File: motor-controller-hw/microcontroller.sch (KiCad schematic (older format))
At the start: 0 parts

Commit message: added more signals and parts
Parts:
- added U?: STM32F303RETx, Package_QFP:LQFP-64_10x10mm_P0.5mm, symbol MotorControllerParts:STM32F303RETx
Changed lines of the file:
@@
 Comment4 ""
 $EndDescr
+$Comp
+L MotorControllerParts:STM32F303RETx U?
+U 1 1 5BC0BBCA
+P 5950 3050
+F 0 "U?" H 5950 3050 50  0000 C CNN
+F 1 "STM32F303RETx" H 5950 2950 50  0000 C CNN
+F 2 "Package_QFP:LQFP-64_10x10mm_P0.5mm" H 5350 1350 50  0001 R CNN
+F 3 "http://www.st.com/st-web-ui/static/active/en/resource/technical/document/datasheet/DM00118585.pdf" H 5950 3050 50  0001 C CNN
+	1    5950 3050
+	1    0    0    -1
+$EndComp
 $EndSCHEMATC

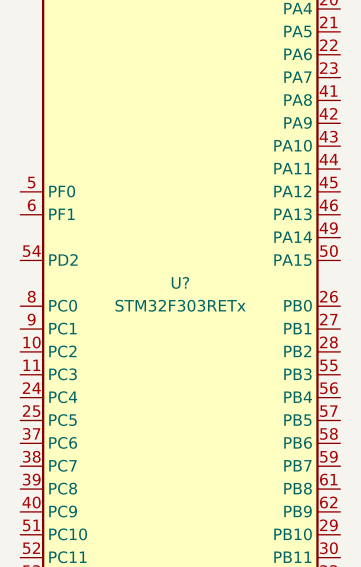
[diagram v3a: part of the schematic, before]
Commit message: Finished Input Protection Added annotations to the title block
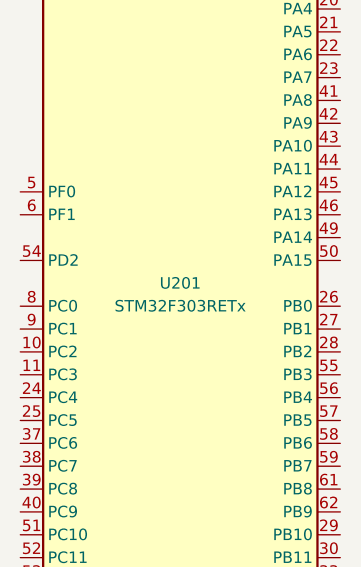
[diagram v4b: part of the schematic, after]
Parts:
- gave numbers to parts that had none: 1
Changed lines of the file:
@@
 $Descr A4 11693 8268
 encoding utf-8
-Sheet 3 5
+Sheet 2 5
 Title ""
 Date ""
 Rev ""
 Comp "Cedarville University"
-Comment1 ""
-Comment2 ""
-Comment3 ""
+Comment1 "Supermileage Motor Controller"
+Comment2 "Senior Design 2018-2019"
+Comment3 "Samuel Ellicott"
 Comment4 ""
 $EndDescr
 $Comp
-L MotorControllerParts:STM32F303RETx U?
+L MotorControllerParts:STM32F303RETx U201
 U 1 1 5BC0BBCA
 P 5950 3050
-F 0 "U?" H 5950 3050 50  0000 C CNN
+F 0 "U201" H 5950 3050 50  0000 C CNN
 F 1 "STM32F303RETx" H 5950 2950 50  0000 C CNN
 F 2 "Package_QFP:LQFP-64_10x10mm_P0.5mm" H 5350 1350 50  0001 R CNN

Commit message: Microcontroller.sch: - Added many labels to pins - Bypass Capacitors - Crystal Oscilator - User Buttons and LEDs
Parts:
- added C? (x4): 100n, symbol Device:C
- added C?: 4u7, symbol Device:C
- added C?: 10n, symbol Device:C
- added C?: 1u, symbol Device:C
- added C? (x2): 26pf, symbol Device:C_Small
- added R?: 390R, symbol Device:R_Small
- added Y?: Crystal, symbol Device:Crystal
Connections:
- net labels added: +3.3V, 3.3v, A_In1, A_In2, A_Out1, A_Out2, CAN_Rx, CAN_Tx, DGND, D_In1, D_In2, D_In3, D_In4, D_Out1, D_Out2, GNDD, MotorTemp, OSC+, OSC-, TMC4671_MISO, TMC4671_MOSI, TMC4671_SCK, TMC4671_SS, Throttle, TransistorTemp, USB_D+, USB_D-
- wire segments 0 -> 81
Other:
- note added: "Bypass Capacitors, one for each Vdd pin, and a 4.7uf cap for good measure.\nAlso two bypass capacitors (1uf and 10nf) for the ADC and DAC."
- note added: "Crystal Oscilator with 18pf load capacitor rating.\nAssumed stray capacitance of 5pf.\nSee: https://www.allaboutcircuits.com/technical-articles/\nchoosing-the-right-oscillator-for-your-microcontroller/"

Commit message: Added system library parts to project library Added a few more comments to IO.sch Added TMC4671 SPI bus as an output for microcontroller.sch Added some connections in the overview page Updated schematic dates
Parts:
- added C? (x2): 100n, symbol MotorControllerParts:C
- added D?: CAN_Status, symbol MotorControllerParts:LED_ALT
- added D?: Heartbeat, symbol MotorControllerParts:LED_ALT
- added D?: User_LED, symbol MotorControllerParts:LED_ALT
- added J?: SWD, symbol MotorControllerParts:Conn_01x06
- added R?: 10K, symbol MotorControllerParts:R
- added R? (x3): 510R, symbol MotorControllerParts:R
- added R?: 4K7, symbol MotorControllerParts:R
- added R?: 100R, symbol MotorControllerParts:R
- added SW?: Reset, symbol MotorControllerParts:SW_Push_45deg
- added SW?: Boot, symbol MotorControllerParts:SW_Push_45deg
- added SW?: User_SW, symbol MotorControllerParts:SW_Push_45deg
- C? (x7): symbol Device:C -> MotorControllerParts:C
- C? (x2): symbol Device:C_Small -> MotorControllerParts:C_Small
- R?: symbol Device:R_Small -> MotorControllerParts:R_Small
- Y?: value Crystal -> 8Mhz; symbol Device:Crystal -> MotorControllerParts:Crystal
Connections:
- net labels added: Boot, CAN_Status, Heartbeat, JTCK, JTMS, Motor_Temp, Reset, SWO, Transistor_Temp, User_LED, User_SW
- wire segments 81 -> 165
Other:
- note added: "Reset and Boot switches for programming the microcontroller with the USB\nbootloader. SWD connector for in system debugging of the microcontroller."
- note added: "User Inputs and Outputs"
- moved on the sheet: U201

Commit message: stuff changed
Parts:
- added J?: User USART, symbol Connector_Generic:Conn_01x03
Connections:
- net labels added: USART_Rx, USART_Tx
- wire segments 165 -> 171
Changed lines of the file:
@@
 	9000 1350 9700 1350
 Wire Notes Line
-	8900 3400 10400 3400
+	8900 2650 10400 2650
 Wire Notes Line
-	10400 3400 10400 6700
+	10400 2650 10400 6700
 Wire Notes Line
 	10400 6700 8900 6700
 Wire Notes Line
-	8900 6700 8900 3400
-Text Notes 9200 3550 0    50   ~ 0
+	8900 6700 8900 2650
+Text Notes 9150 2750 0    50   ~ 0
 User Inputs and Outputs
+Text Label 6400 1550 2    50   ~ 0
+USART_Tx
+Text Label 6400 1650 2    50   ~ 0
+USART_Rx
+Wire Wire Line
+	6400 1550 5700 1550
+Wire Wire Line
+	6400 1650 5700 1650
+$Comp
+L Connector_Generic:Conn_01x03 J?
+U 1 1 5BF48BC7
+P 9950 3100
+F 0 "J?" H 9900 3300 50  0000 L CNN
+F 1 "User USART" H 9750 2900 50  0000 L CNN
+F 2 "" H 9950 3100 50  0001 C CNN
+F 3 "~" H 9950 3100 50  0001 C CNN
+	1    9950 3100
+	1    0    0    -1
+$EndComp
+$Comp
+L MotorControllerParts:GNDD #PWR?
+U 1 1 5BF68017
+P 9650 3400
+F 0 "#PWR?" H 9650 3150 50  0001 C CNN
+F 1 "GNDD" H 9654 3245 50  0000 C CNN
+F 2 "" H 9650 3400 50  0001 C CNN
+F 3 "" H 9650 3400 50  0001 C CNN
+	1    9650 3400
+	1    0    0    -1
+$EndComp
+Text Label 9000 3100 0    50   ~ 0
+USART_Tx
+Text Label 9000 3200 0    50   ~ 0
+USART_Rx
+Wire Wire Line
+	9650 3400 9650 3000
+Wire Wire Line
+	9650 3000 9750 3000
+Wire Wire Line
+	9000 3100 9750 3100
+Wire Wire Line
+	9000 3200 9750 3200
 $EndSCHEMATC

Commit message: microcontroller.sch: added some more outputs to the TMC4671 schematic
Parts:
- J?: symbol Connector_Generic:Conn_01x03 -> MotorControllerParts:Conn_01x03
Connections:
- net labels added: ~TMC4671_SS
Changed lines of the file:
@@
 $Descr USLetter 11000 8500
 encoding utf-8
-Sheet 2 5
+Sheet 2 4
 Title "STM32 Microcontroller"
 Date "2018-11-17"
@@
 Wire Wire Line
 	2850 5400 3250 5400
-Wire Wire Line
-	3250 5200 2850 5200
-Wire Wire Line
-	2850 5200 2850 5400
-Connection ~ 2850 5400
 Text Label 6400 3350 2    50   ~ 0
 SWO
@@
 	9000 4250 9650 4250
 Text HLabel 9700 1350 2    50   Output ~ 0
-TMC4671_SS
+~TMC4671_SS
 Text HLabel 9700 1450 2    50   Output ~ 0
 TMC4671_SCK
-Text HLabel 9700 1550 2    50   Input ~ 0
+Text HLabel 9700 1650 2    50   Input ~ 0
 TMC4671_MISO
-Text HLabel 9700 1650 2    50   Input ~ 0
+Text HLabel 9700 1550 2    50   Output ~ 0
+TMC4671_MOSI
+Text Label 9000 1550 0    50   ~ 0
 TMC4671_MOSI
 Text Label 9000 1650 0    50   ~ 0
-TMC4671_MOSI
-Text Label 9000 1550 0    50   ~ 0
 TMC4671_MISO
 Text Label 9000 1450 0    50   ~ 0
@@
 TMC4671_SS
 Wire Wire Line
+	9000 1550 9700 1550
+Wire Wire Line
 	9000 1650 9700 1650
-Wire Wire Line
-	9000 1550 9700 1550
 Wire Wire Line
 	9000 1450 9700 1450
@@
 	6400 1650 5700 1650
 $Comp
-L Connector_Generic:Conn_01x03 J?
+L MotorControllerParts:Conn_01x03 J?
 U 1 1 5BF48BC7
 P 9950 3100
@@
 Wire Wire Line
 	9000 3200 9750 3200
+$Comp
+L MotorControllerParts:+3.3V #PWR?
+U 1 1 5BFBCA2F
+P 2850 5050
+F 0 "#PWR?" H 2850 4900 50  0001 C CNN
+F 1 "+3.3V" H 2865 5223 50  0000 C CNN
+F 2 "" H 2850 5050 50  0001 C CNN
+F 3 "" H 2850 5050 50  0001 C CNN
+	1    2850 5050
+	1    0    0    -1
+$EndComp
+Wire Wire Line
+	2850 5050 2850 5200
+Wire Wire Line
+	2850 5200 3250 5200
 $EndSCHEMATC
